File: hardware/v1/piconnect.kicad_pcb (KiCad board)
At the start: 2 copper layers, 96.5 x 109.2 mm, 54 parts, among them CON1 BARREL_JACK, CON2 BARREL_JACK, P1 CONN_01X04, P10 CONN_01X04, P11 CONN_01X04, P12 CONN_01X04, P13 CONN_01X04, P14 CONN_01X04, P15 CONN_01X04, P16 CONN_01X04, P17 CONN_01X04, P18 CONN_01X04, P19 CONN_01X05, P2 CONN_01X04, P20 CONN_02X05, P21 CONN_02X05, P22 CONN_02X05, P23 CONN_02X05, P24 CONN_02X05, P25 CONN_02X05, P26 CONN_02X05, P27 CONN_02X05, P28 CONN_01X03, P29 CONN_01X03, P3 CONN_01X04, P30 CONN_01X04, P4 CONN_01X04, P5 CONN_01X04, P6 CONN_01X04, P7 CONN_01X04, P8 CONN_01X04, P9 CONN_01X04, Q1 2N7000, Q2 2N7000, Q3 2N7000, U1 Pi2_Connector, U2 MAX7221, U3 MAX7221

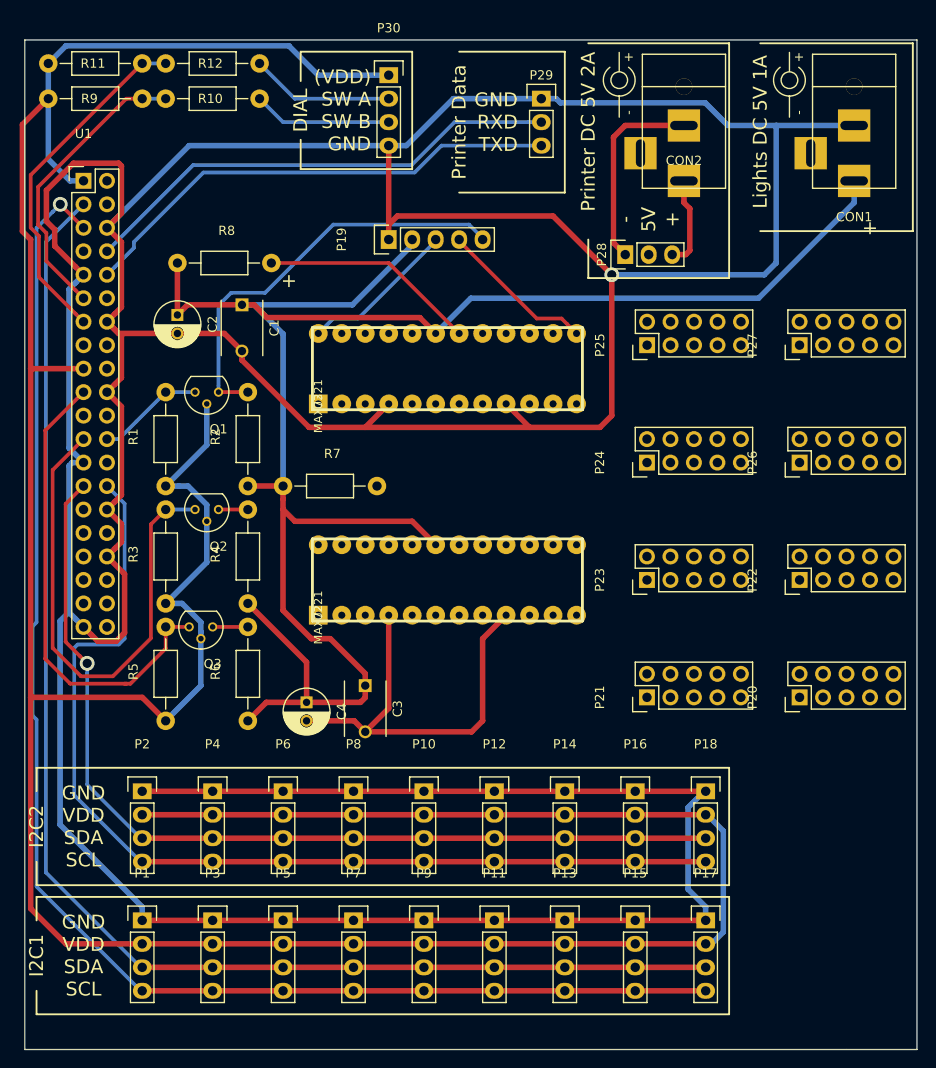
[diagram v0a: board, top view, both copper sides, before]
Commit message: Finish routing of piconnect board and generate gerber files
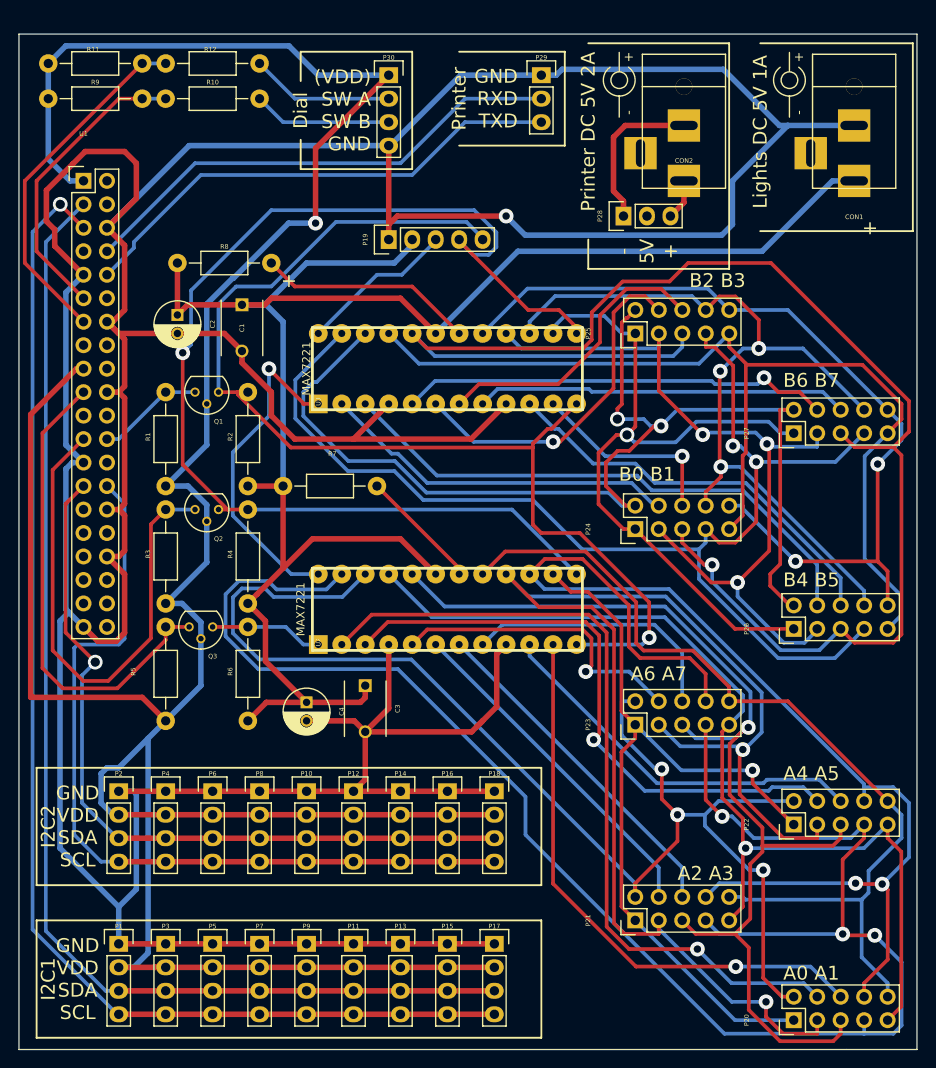
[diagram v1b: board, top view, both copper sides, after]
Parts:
- moved P20 34.9 mm to (95.9, 194.9)
- moved P22 26.5 mm to (95.9, 173.8)
- moved P21 24.2 mm to (78.7, 184.2)
- moved P17 23.0 mm to (63.5, 186.7)
- moved P18 22.9 mm to (63.5, 170.2)
- moved P15 20.5 mm to (58.4, 186.7)
- moved P16 20.3 mm to (58.4, 170.2)
- moved P26 18.0 mm to (95.9, 152.6)
- moved P13 18.0 mm to (53.3, 186.7)
- moved P14 17.8 mm to (53.3, 170.2)
- moved P23 15.7 mm to (78.7, 163.0)
- moved P11 15.5 mm to (48.3, 186.7)
- moved P12 15.2 mm to (48.3, 170.2)
- moved P9 13.0 mm to (43.2, 186.7)
- moved P10 12.7 mm to (43.2, 170.2)
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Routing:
- net /A_SEGD: track 0.00 -> 184.3 mm, vias 0 -> 3
- net /B_SEGC: track 0.00 -> 163.9 mm, vias 0 -> 1
- net /A_SEGB: track 0.00 -> 145.0 mm, vias 0 -> 2
- net /A_SEGDP: track 0.00 -> 142.1 mm, vias 0 -> 3
- net /B_SEGD: track 0.00 -> 132.9 mm, vias 0 -> 2
- net /A_SEGF: track 0.00 -> 126.7 mm, vias 0 -> 2
- net /B_SEGDP: track 0.00 -> 123.2 mm, vias 0 -> 2
- net /A_SEGC: track 0.00 -> 118.7 mm, vias 0 -> 1
- net /A_SEGE: track 0.00 -> 109.7 mm, vias 0 -> 1
- net /CLK_5V: track 20.2 -> 129.5 mm, vias 0 -> 1
- net /B_SEGE: track 0.00 -> 109.0 mm
- net /A_SEGG: track 0.00 -> 98.7 mm
- net /B_SEGG: track 0.00 -> 93.3 mm, vias 0 -> 2
- net /B_SEGF: track 0.00 -> 89.9 mm, vias 0 -> 3
- net /A_DIG0: track 0.00 -> 88.5 mm, vias 0 -> 1
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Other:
- board size 96.5 x 109.2 mm -> 97.2 x 109.9 mm
- board text added: "A0 A1"
- board text added: "A2 A3"
- board text added: "A4 A5"
- board text added: "A6 A7"
- board text added: "B0 B1"
- board text added: "B2 B3"
- board text added: "B4 B5"
- board text added: "B6 B7"
- board text added: "Dial"
- board text added: "Printer"
- board text added: "REDEUCE piconnector v1 2016-08-12 Kristian Hentschel"
- board text removed: "DIAL"
- board text removed: "Printer Data"

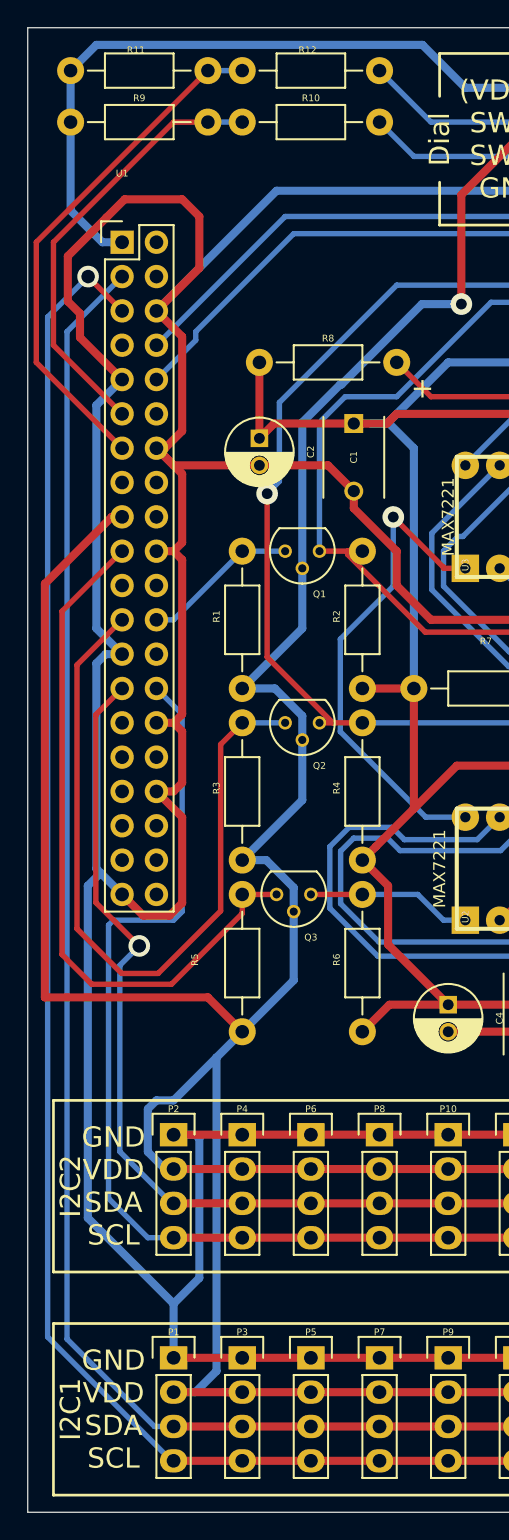
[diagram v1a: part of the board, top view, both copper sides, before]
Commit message: Add mosfet clock gates to I2C connector rows - because addresses conflict and the second bus (I2C0) cannot be used safely on the raspberry pi.
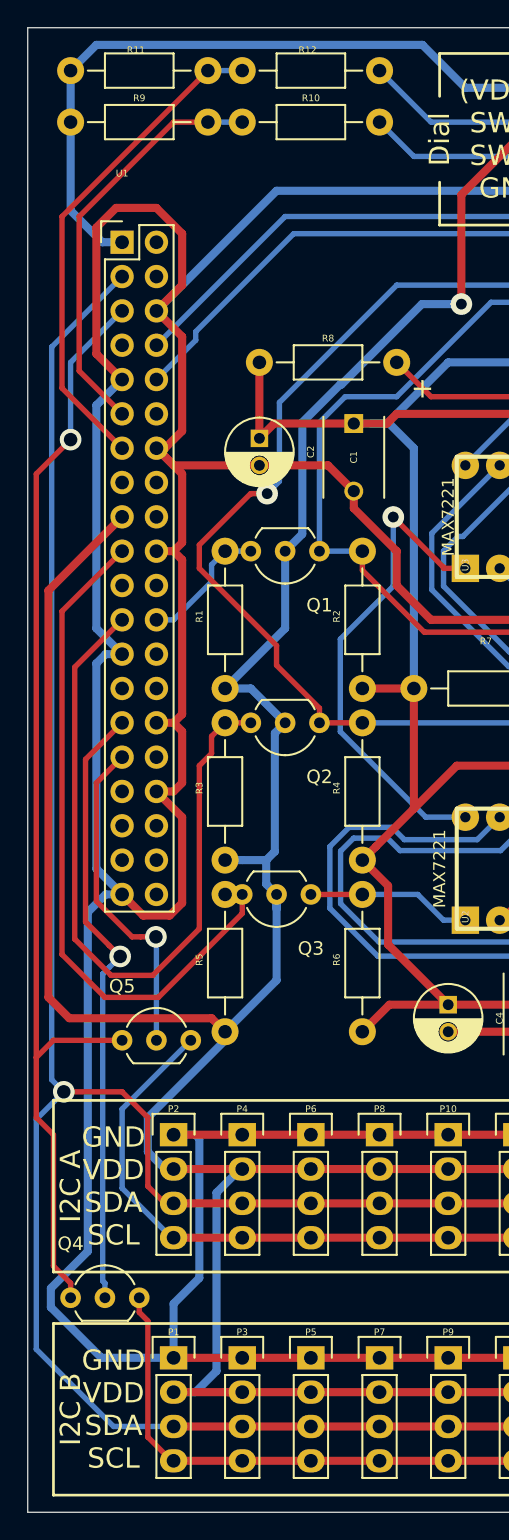
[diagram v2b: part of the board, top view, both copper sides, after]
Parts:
- added Q4: 2N7000, TO_SOT_Packages_THT:TO-92_Inline_Wide, F.Cu at (15.2, 182.2)
- added Q5: 2N7000, TO_SOT_Packages_THT:TO-92_Inline_Wide, F.Cu at (19.1, 163.2)
- Q1, Q2, Q3: footprint TO_SOT_Packages_THT:TO-92_Molded_Narrow -> TO_SOT_Packages_THT:TO-92_Inline_Wide
- moved R1 1.27 mm to (26.7, 137.2)
- moved R3 1.27 mm to (26.7, 149.9)
- moved R5 1.27 mm to (26.7, 162.6)
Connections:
- net /A_DIG0 renamed /sheet57A5CF13/DIG0
- net /A_DIG1 renamed /sheet57A5CF13/DIG1
- net /A_DIG2 renamed /sheet57A5CF13/DIG2
- net /A_DIG3 renamed /sheet57A5CF13/DIG3
- net /A_DIG4 renamed /sheet57A5CF13/DIG4
- net /A_DIG5 renamed /sheet57A5CF13/DIG5
- net /A_DIG6 renamed /sheet57A5CF13/DIG6
- net /A_DIG7 renamed /sheet57A5CF13/DIG7
- net /A_SEGA renamed /sheet57A5CF13/SEGA
- net /A_SEGB renamed /sheet57A5CF13/SEGB
- net /A_SEGC renamed /sheet57A5CF13/SEGC
- net /A_SEGD renamed /sheet57A5CF13/SEGD
- net /A_SEGDP renamed /sheet57A5CF13/SEGDP
- net /A_SEGE renamed /sheet57A5CF13/SEGE
- net /A_SEGF renamed /sheet57A5CF13/SEGF
- net /A_SEGG renamed /sheet57A5CF13/SEGG
- net /B_DIG0 renamed /sheet57A5D898/DIG0
- net /B_DIG1 renamed /sheet57A5D898/DIG1
- net /B_DIG2 renamed /sheet57A5D898/DIG2
- net /B_DIG3 renamed /sheet57A5D898/DIG3
- net /B_DIG4 renamed /sheet57A5D898/DIG4
- net /B_DIG5 renamed /sheet57A5D898/DIG5
- net /B_DIG6 renamed /sheet57A5D898/DIG6
- net /B_DIG7 renamed /sheet57A5D898/DIG7
- net /B_SEGA renamed /sheet57A5D898/SEGA
- net /B_SEGB renamed /sheet57A5D898/SEGB
- net /B_SEGC renamed /sheet57A5D898/SEGC
- net /B_SEGD renamed /sheet57A5D898/SEGD
- net /B_SEGDP renamed /sheet57A5D898/SEGDP
- net /B_SEGE renamed /sheet57A5D898/SEGE
- net /B_SEGF renamed /sheet57A5D898/SEGF
- net /B_SEGG renamed /sheet57A5D898/SEGG
- net /CLK_5V renamed /sheet57A5CF13/CLK_5V
- net /CS_5V renamed /sheet57A33FA6/CMOS_OUT
- net /DIN_5V renamed /sheet57A33FA8/CMOS_OUT
- net /DOUT1_5V renamed /sheet57A5D898/DIN_5V
- net /DOUT2_5V renamed /sheet57A5D898/DOUT_5V
- net /SPI0_CE0 renamed /sheet57A33FA6/TTL_IN
- net /SPI0_MOSI renamed /sheet57A33FA8/TTL_IN
- net /SPI0_SCLK renamed /sheet57A33FA7/TTL_IN
- P1 pad 4: /I2C1_SCL -> Net-(P1-Pad4)
- P10 pad 3: /I2C2_SDA -> /I2C1_SDA
- P10 pad 4: /I2C2_SCL -> Net-(P10-Pad4)
- P11 pad 4: /I2C1_SCL -> Net-(P1-Pad4)
- P12 pad 3: /I2C2_SDA -> /I2C1_SDA
- P12 pad 4: /I2C2_SCL -> Net-(P10-Pad4)
- P13 pad 4: /I2C1_SCL -> Net-(P1-Pad4)
- P14 pad 3: /I2C2_SDA -> /I2C1_SDA
- P14 pad 4: /I2C2_SCL -> Net-(P10-Pad4)
- P15 pad 4: /I2C1_SCL -> Net-(P1-Pad4)
- P16 pad 3: /I2C2_SDA -> /I2C1_SDA
- P16 pad 4: /I2C2_SCL -> Net-(P10-Pad4)
- P17 pad 4: /I2C1_SCL -> Net-(P1-Pad4)
- P18 pad 3: /I2C2_SDA -> /I2C1_SDA
- P18 pad 4: /I2C2_SCL -> Net-(P10-Pad4)
- P2 pad 3: /I2C2_SDA -> /I2C1_SDA
- P2 pad 4: /I2C2_SCL -> Net-(P10-Pad4)
- P3 pad 4: /I2C1_SCL -> Net-(P1-Pad4)
- P4 pad 3: /I2C2_SDA -> /I2C1_SDA
- P4 pad 4: /I2C2_SCL -> Net-(P10-Pad4)
- P5 pad 4: /I2C1_SCL -> Net-(P1-Pad4)
- P6 pad 3: /I2C2_SDA -> /I2C1_SDA
- P6 pad 4: /I2C2_SCL -> Net-(P10-Pad4)
- P7 pad 4: /I2C1_SCL -> Net-(P1-Pad4)
- P8 pad 3: /I2C2_SDA -> /I2C1_SDA
- P8 pad 4: /I2C2_SCL -> Net-(P10-Pad4)
- P9 pad 4: /I2C1_SCL -> Net-(P1-Pad4)
- U1 pad 27: /I2C2_SDA -> (no net)
- U1 pad 28: /I2C2_SCL -> (no net)
- U1 pad 29: (no net) -> /EN_I2C0_1
- U1 pad 31: (no net) -> /EN_I2C0_2
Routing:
- net /I2C2_SCL: track 90.0 -> 0.00 mm
- net /I2C2_SDA: track 83.2 -> 0.00 mm, vias 1 -> 0
- net /I2C1_SDA: track 131.5 -> 191.4 mm, vias 0 -> 1
- net Net-(P10-Pad4): track 0.00 -> 59.0 mm
- net Net-(P1-Pad4): track 0.00 -> 53.8 mm
- net /I2C1_SCL: track 137.0 -> 83.6 mm
- net /EN_I2C0_1: track 0.00 -> 45.3 mm, vias 0 -> 1
- net /EN_I2C0_2: track 0.00 -> 24.6 mm, vias 0 -> 1
- net VDD: track 323.5 -> 313.5 mm
- net /sheet57A5CF13/CLK_5V: track 129.5 -> 133.9 mm
- net GND: track 524.6 -> 528.9 mm
- net /sheet57A33FA6/TTL_IN: track 11.6 -> 9.83 mm
- net /GPIO_BCM17: track 32.5 -> 30.9 mm
- net /GPIO_BCM27: track 38.4 -> 36.8 mm
- net /sheet57A33FA7/TTL_IN: track 55.9 -> 54.8 mm
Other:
- board text added: "I2C A"
- board text added: "I2C B"
- board text removed: "I2C1"
- board text removed: "I2C2"
